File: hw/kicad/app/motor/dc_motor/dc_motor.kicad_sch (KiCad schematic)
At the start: 23 parts, among them J1 TOP, J2 Motor 1, J3 Motor 2, J4 Motor 3, J6 BOTTUM, U1 DRV8870DDA, U2 DRV8870DDA, U3 DRV8870DDA

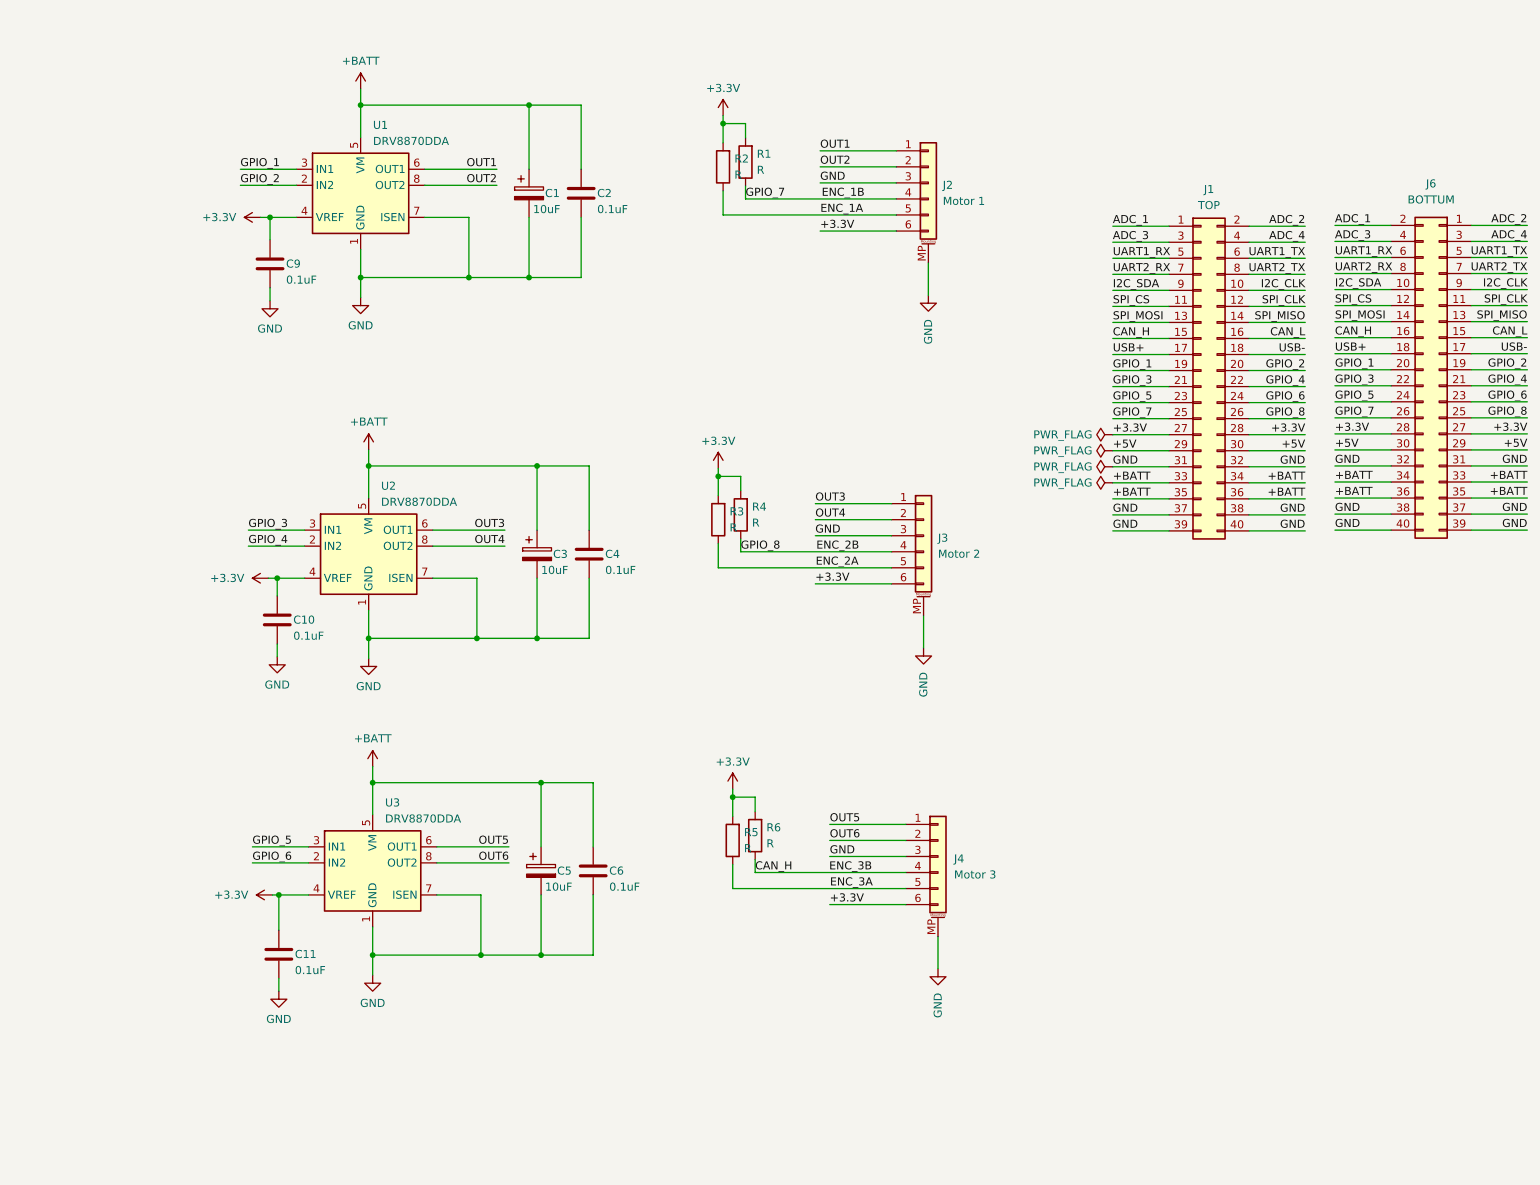
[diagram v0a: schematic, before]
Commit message: 尽力改成40mmx40mm
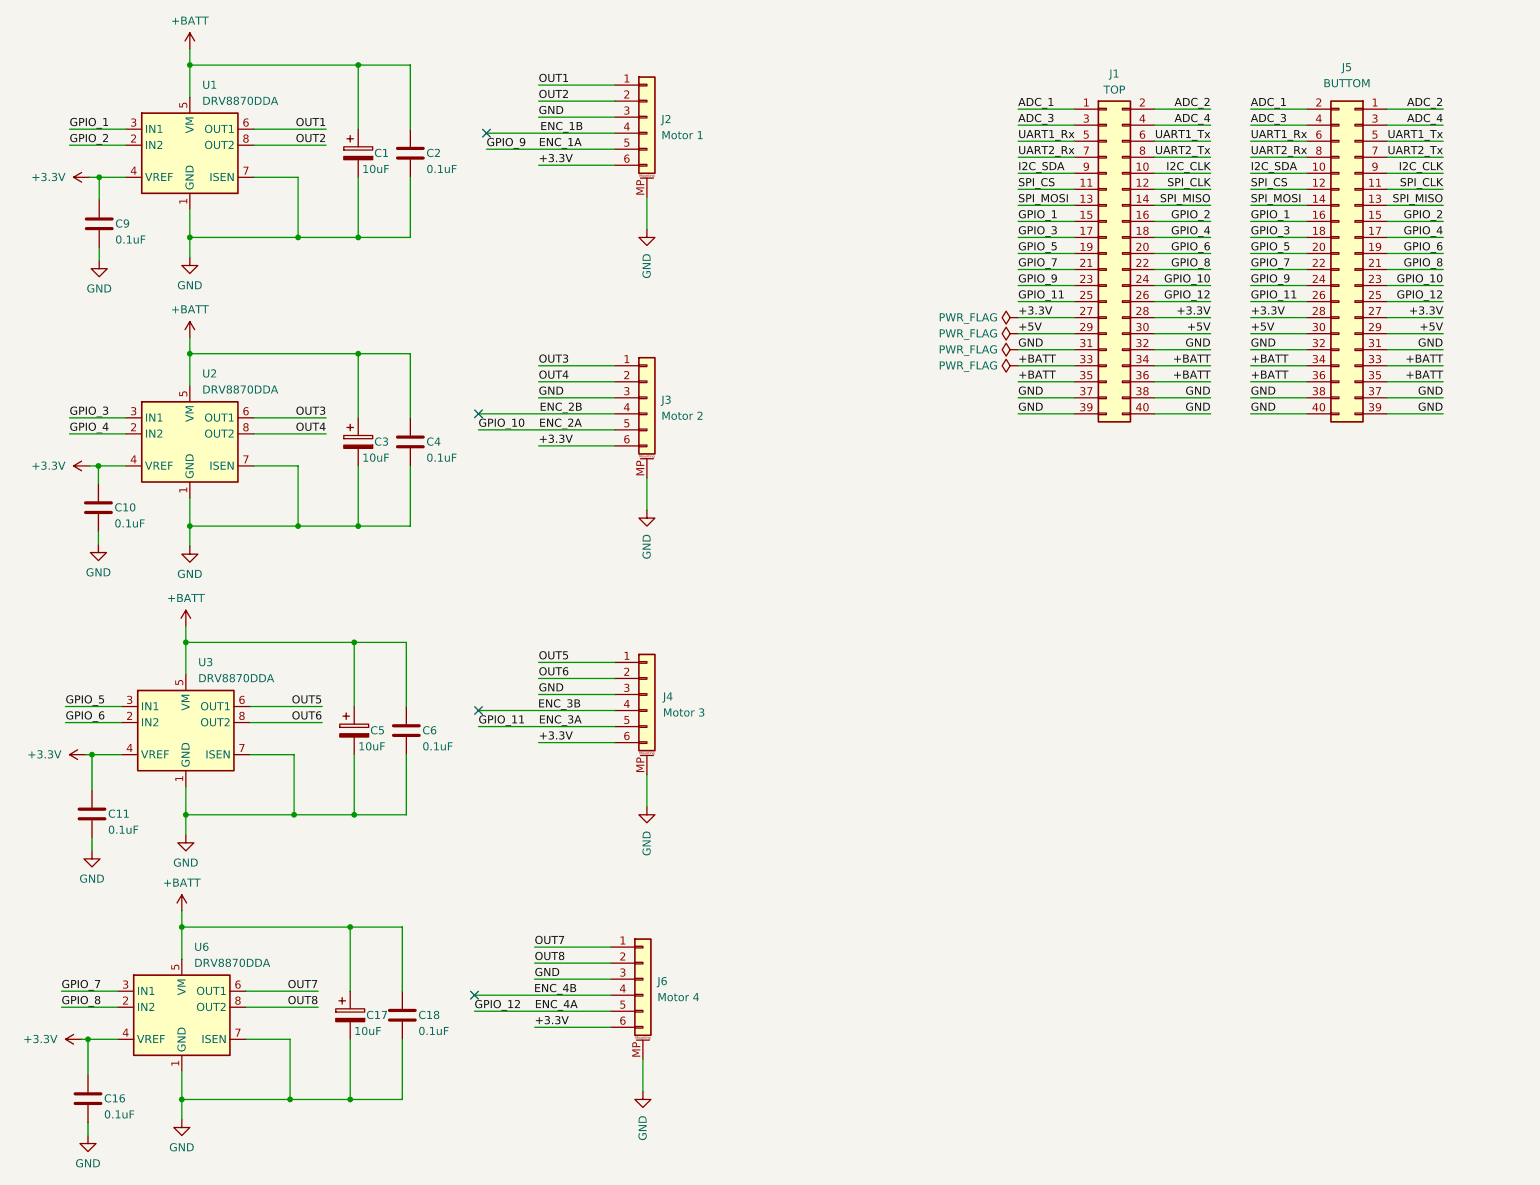
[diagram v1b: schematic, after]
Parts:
- removed J6: BOTTUM, Connector_PinHeader_1.27mm:PinHeader_2x20_P1.27mm_Vertical_SMD, symbol Connector_Generic:Conn_02x20_Odd_Even
- removed R1, R2, R3, R4, R5, R6: R, Resistor_SMD:R_0805_2012Metric, symbol Device:R
- added C16, C18: 0.1uF, Capacitor_SMD:C_0805_2012Metric, symbol Device:C
- added C17: 10uF, Capacitor_SMD:C_1210_3225Metric, symbol Device:C_Polarized
- added J5: BUTTOM, Connector_PinHeader_1.27mm:PinHeader_2x20_P1.27mm_Vertical_SMD, symbol Connector_Generic:Conn_02x20_Odd_Even
- added J6: Motor 4, Connector_JST:JST_GH_SM06B-GHS-TB_1x06-1MP_P1.25mm_Horizontal, symbol Connector_Generic_MountingPin:Conn_01x06_MountingPin
- added U6: DRV8870DDA, Package_SO:Texas_HTSOP-8-1EP_3.9x4.9mm_P1.27mm_EP2.95x4.9mm_Mask2.4x3.1mm_ThermalVias, symbol Driver_Motor:DRV8870DDA
- C1, C3, C5: footprint Capacitor_SMD:CP_Elec_6.3x5.4 -> Capacitor_SMD:C_1210_3225Metric
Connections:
- net CAN_L is gone; now on net GPIO_2: J1.16 (Pin_16)
- net USB+ is gone; now on net GPIO_3: J1.17 (Pin_17)
- net USB- is gone; now on net GPIO_4: J1.18 (Pin_18)
- net +3.3V: now also C16.1, J5.27 (Pin_27), J5.28 (Pin_28), J6.6 (Pin_6), U6.4 (VREF)
- net +5V: now also J5.29 (Pin_29), J5.30 (Pin_30)
- net +BATT: now also C17.1, C18.1, J5.33 (Pin_33), J5.34 (Pin_34), J5.35 (Pin_35), J5.36 (Pin_36), U6.5 (VM)
- net ADC_1: now also J5.2 (Pin_2)
- net ADC_2: now also J5.1 (Pin_1)
- net ADC_3: now also J5.4 (Pin_4)
- net ADC_4: now also J5.3 (Pin_3)
- net ENC_1A: now also J1.23 (Pin_23), J5.24 (Pin_24)
- net ENC_1B: no longer J1.25 (Pin_25)
- net ENC_2A: now also J1.24 (Pin_24), J5.23 (Pin_23)
- net ENC_2B: no longer J1.26 (Pin_26)
- net ENC_3A: now also J1.25 (Pin_25), J5.26 (Pin_26)
- net GND: now also C16.2, C17.2, C18.2, J5.31 (Pin_31), J5.32 (Pin_32), J5.37 (Pin_37), J5.38 (Pin_38), J5.39 (Pin_39), J5.40 (Pin_40), J6.3 (Pin_3), J6.MP (MountPin), U6.1 (GND), U6.7 (ISEN), U6.9 (GND)
- net GPIO_1: now also J1.15 (Pin_15), J5.16 (Pin_16); no longer J1.19 (Pin_19)
- net GPIO_2: now also J5.15 (Pin_15); no longer J1.20 (Pin_20)
- net GPIO_3: now also J5.18 (Pin_18); no longer J1.21 (Pin_21)
- net GPIO_4: now also J5.17 (Pin_17); no longer J1.22 (Pin_22)
- net GPIO_5: now also J1.19 (Pin_19), J5.20 (Pin_20); no longer J1.23 (Pin_23)
- net GPIO_6: now also J1.20 (Pin_20), J5.19 (Pin_19); no longer J1.24 (Pin_24)
- net I2C_CLK: now also J5.9 (Pin_9)
- net I2C_SDA: now also J5.10 (Pin_10)
- net SPI_CLK: now also J5.11 (Pin_11)
- net SPI_CS: now also J5.12 (Pin_12)
- net SPI_MISO: now also J5.13 (Pin_13)
- net SPI_MOSI: now also J5.14 (Pin_14)
- net CAN_H renamed ENC_3B
- net ENC_3B: no longer J1.15 (Pin_15)
- net UART1_RX renamed UART1_Rx
- net UART1_Rx: now also J5.6 (Pin_6)
- net UART1_TX renamed UART1_Tx
- net UART1_Tx: now also J5.5 (Pin_5)
- net UART2_RX renamed UART2_Rx
- net UART2_Rx: now also J5.8 (Pin_8)
- net UART2_TX renamed UART2_Tx
- net UART2_Tx: now also J5.7 (Pin_7)
- new net ENC_4A: J1.26 (Pin_26), J5.25 (Pin_25), J6.5 (Pin_5)
- new net ENC_4B: J6.4 (Pin_4)
- new net GPIO_7: J1.21 (Pin_21), J5.22 (Pin_22), U6.3 (IN1)
- new net GPIO_8: J1.22 (Pin_22), J5.21 (Pin_21), U6.2 (IN2)
- new net OUT7: J6.1 (Pin_1), U6.6 (OUT1)
- new net OUT8: J6.2 (Pin_2), U6.8 (OUT2)
- no-connect marks 0 -> 4
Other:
- moved on the sheet: C1, C10, C11, C2, C3, C4, C5, C6, C9, J2, J3, J4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

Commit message: Merge from normal
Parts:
- C1, C17, C3, C5: footprint Capacitor_SMD:C_1210_3225Metric -> Capacitor_SMD:CP_Elec_6.3x5.4
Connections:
- net ENC_1B is gone; now on net GND: J2.4 (Pin_4)
- net ENC_2B is gone; now on net GND: J3.4 (Pin_4)
- net ENC_3B is gone; now on net GND: J4.4 (Pin_4)
- net ENC_4B is gone; now on net GND: J6.4 (Pin_4)
- net +3.3V: now also J2.1 (Pin_1), J3.1 (Pin_1), J4.1 (Pin_1), J6.1 (Pin_1); no longer J2.6 (Pin_6), J3.6 (Pin_6), J4.6 (Pin_6), J6.6 (Pin_6)
- net ENC_1A: now also J2.2 (Pin_2); no longer J2.5 (Pin_5)
- net ENC_2A: now also J3.2 (Pin_2); no longer J3.5 (Pin_5)
- net ENC_3A: now also J4.2 (Pin_2); no longer J4.5 (Pin_5)
- net ENC_4A: now also J6.2 (Pin_2); no longer J6.5 (Pin_5)
- net GND: no longer J2.3 (Pin_3), J3.3 (Pin_3), J4.3 (Pin_3), J6.3 (Pin_3)
- net OUT1: now also J2.5 (Pin_5); no longer J2.1 (Pin_1)
- net OUT2: now also J2.6 (Pin_6); no longer J2.2 (Pin_2)
- net OUT3: now also J3.5 (Pin_5); no longer J3.1 (Pin_1)
- net OUT4: now also J3.6 (Pin_6); no longer J3.2 (Pin_2)
- net OUT5: now also J4.5 (Pin_5); no longer J4.1 (Pin_1)
- net OUT6: now also J4.6 (Pin_6); no longer J4.2 (Pin_2)
- net OUT7: now also J6.5 (Pin_5); no longer J6.1 (Pin_1)
- net OUT8: now also J6.6 (Pin_6); no longer J6.2 (Pin_2)
